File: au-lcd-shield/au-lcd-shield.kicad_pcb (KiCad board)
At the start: 2 copper layers, 65 x 45 mm, 14 parts, among them IC1 ME6206A15M3G, J1 Power, J2 Backlight, J4 Conn_02x09_Odd_Even, U1 UA78M33CDCYR

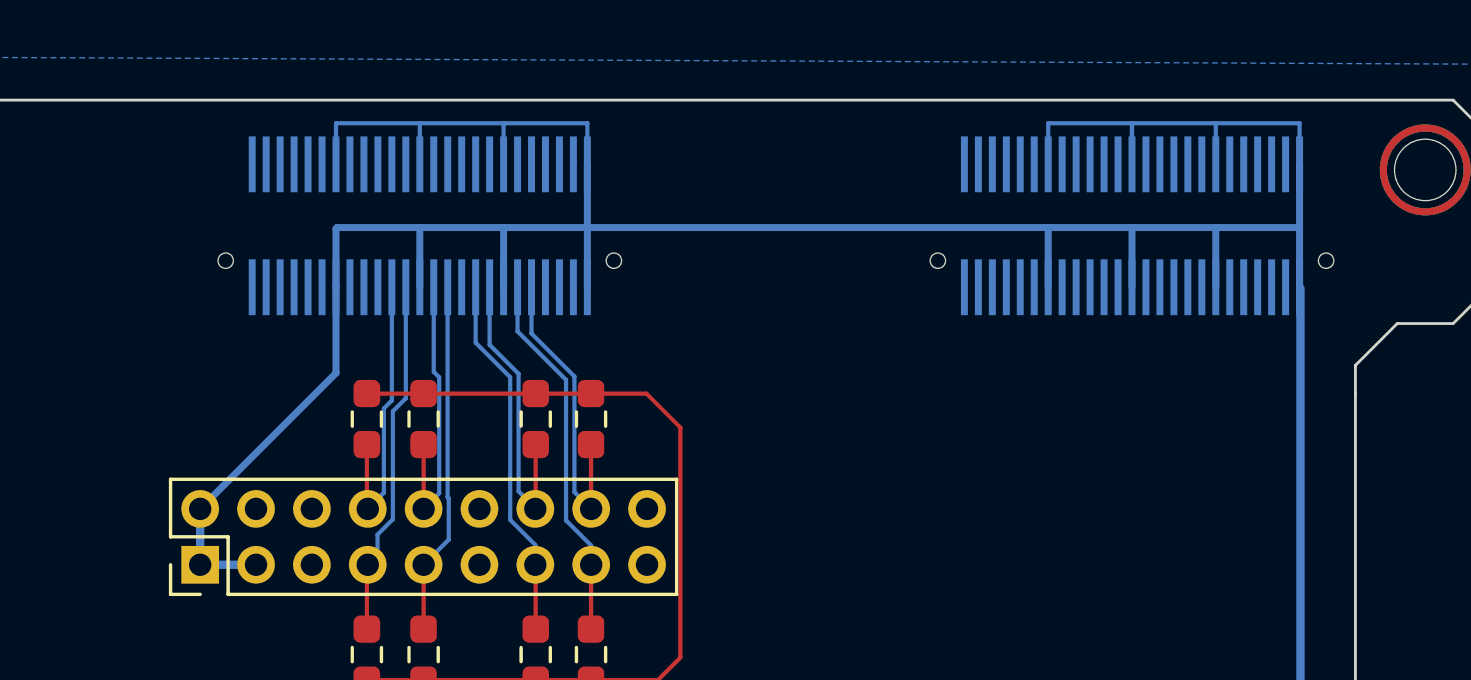
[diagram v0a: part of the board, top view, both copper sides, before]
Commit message: reroute 3.3v traces
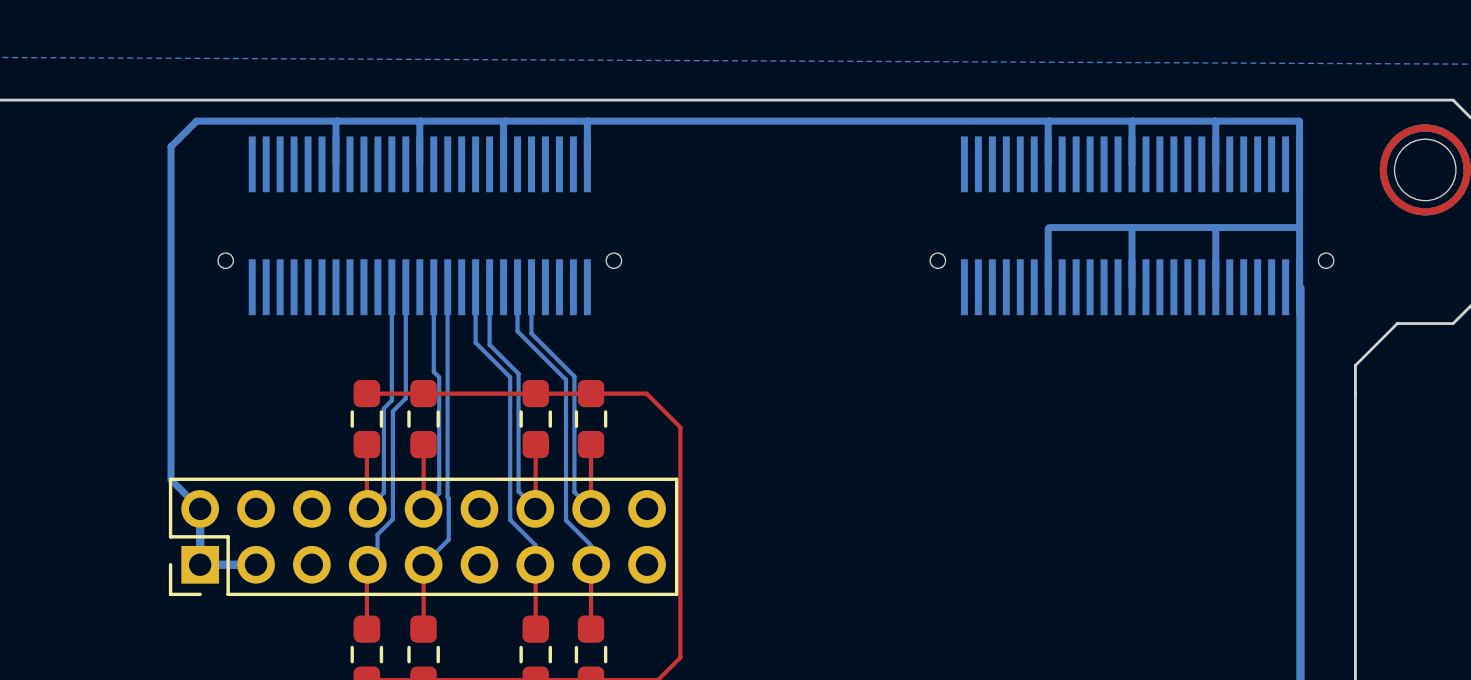
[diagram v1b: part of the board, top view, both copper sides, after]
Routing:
- net +3.3V: track 215.9 -> 207.1 mm
